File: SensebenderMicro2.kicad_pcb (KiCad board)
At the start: 2 copper layers, 19 x 32 mm, 39 parts, among them P1 Debug, P2 MYSX_1.2, P3 Antenna, Q1 SI2333DDS-T1-GE3, U1 ATSAMD21E, U2 MCP1703T-3302E, U3 NRF24L01, U4 RFM69HW, U5 ATSHA204A, U6 AT45DB041E, U7 Si7021, U8 AT24C32-STUM-T, Y1 32Khz

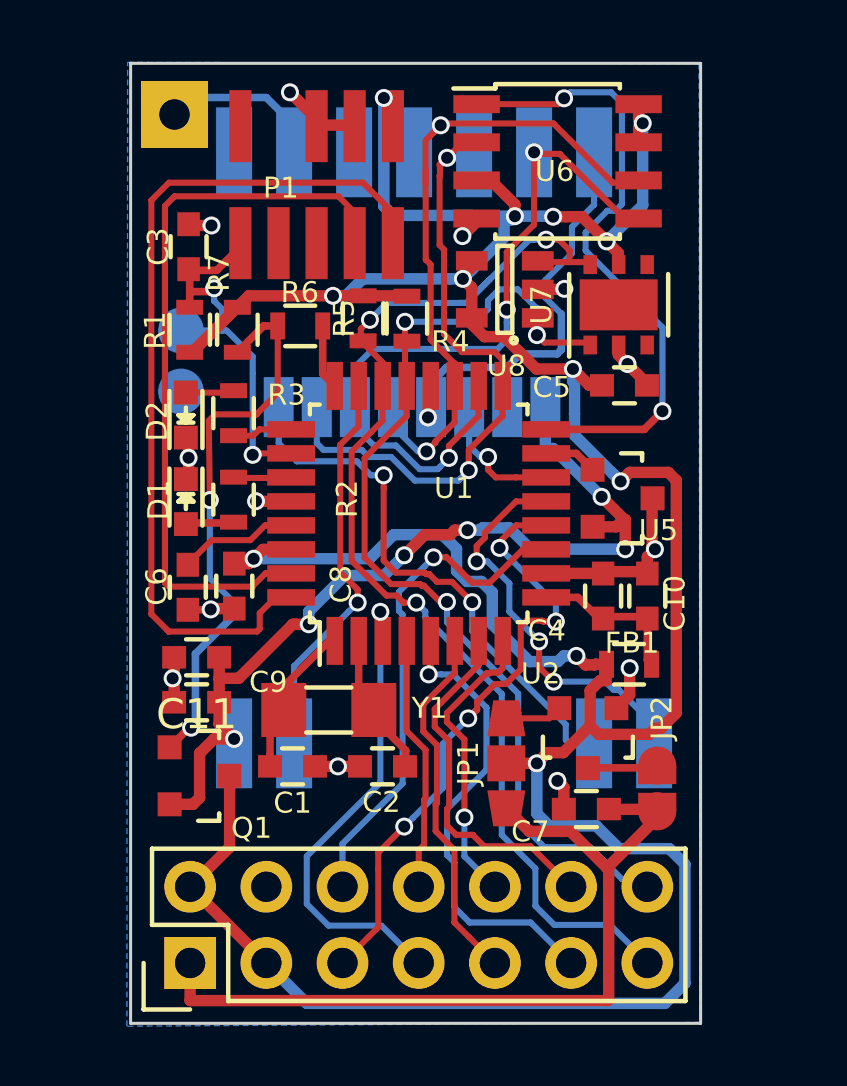
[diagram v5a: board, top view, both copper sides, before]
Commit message: Updated to use MYSX2.x with reset
Also shuffled peripherals around on the samd, to make routing easier
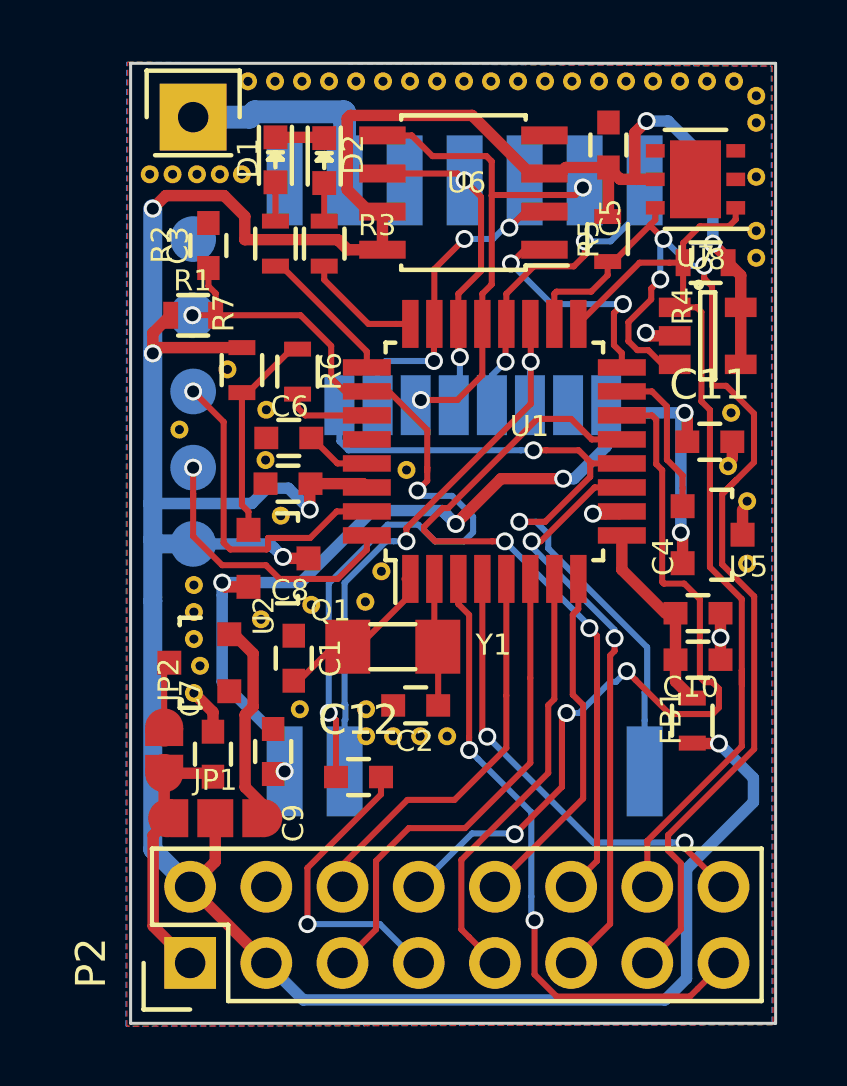
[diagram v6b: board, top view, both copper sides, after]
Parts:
- removed P1: Debug, mysensors_connectors:Cortex_M_Debug_Connector
- added C12: C, Capacitors_SMD:C_0603, F.Cu at (96.6, 105.8)
- added REF**: via-0.6mm, mysensors_obscurities:via-0.6mm, F.Cu at (108.9, 95.4)
- added REF**: via-0.6mm, mysensors_obscurities:via-0.6mm, F.Cu at (93.5, 93.5)
- added REF**: via-0.6mm, mysensors_obscurities:via-0.6mm, F.Cu at (93.5, 95.2)
- added REF**: via-0.6mm, mysensors_obscurities:via-0.6mm, F.Cu at (98.2, 95.6)
- added REF**: via-0.6mm, mysensors_obscurities:via-0.6mm, F.Cu at (99.6, 104.4)
- added REF**: via-0.6mm, mysensors_obscurities:via-0.6mm, F.Cu at (98.7, 104.4)
- added REF**: via-0.6mm, mysensors_obscurities:via-0.6mm, F.Cu at (97.8, 104.4)
- added REF**: via-0.6mm, mysensors_obscurities:via-0.6mm, F.Cu at (96.9, 104.4)
- added REF**: via-0.6mm, mysensors_obscurities:via-0.6mm, F.Cu at (92.2, 92.2)
- added REF**: via-0.6mm, mysensors_obscurities:via-0.6mm, F.Cu at (90.6, 94.2)
- added REF**: via-0.6mm, mysensors_obscurities:via-0.6mm, F.Cu at (91.1, 103.0)
- added REF**: via-0.6mm, mysensors_obscurities:via-0.6mm, F.Cu at (109.0, 93.6)
- added REF**: via-0.6mm, mysensors_obscurities:via-0.6mm, F.Cu at (91.3, 102.1)
- added REF**: via-0.6mm, mysensors_obscurities:via-0.6mm, F.Cu at (91.1, 101.2)
- added REF**: via-0.6mm, mysensors_obscurities:via-0.6mm, F.Cu at (91.1, 100.3)
- added REF**: via-0.6mm, mysensors_obscurities:via-0.6mm, F.Cu at (91.1, 99.4)
- added REF**: via-0.6mm, mysensors_obscurities:via-0.6mm, F.Cu at (97.4, 98.9)
- added REF**: via-0.6mm, mysensors_obscurities:via-0.6mm, F.Cu at (96.8, 99.9)
- added REF**: via-0.6mm, mysensors_obscurities:via-0.6mm, F.Cu at (93.3, 100.5)
- added REF**: via-0.6mm, mysensors_obscurities:via-0.6mm, F.Cu at (95.0, 100.1)
- added REF**: via-0.6mm, mysensors_obscurities:via-0.6mm, F.Cu at (96.9, 103.5)
- added REF**: via-0.6mm, mysensors_obscurities:via-0.6mm, F.Cu at (94.6, 103.5)
- added REF**: via-0.6mm, mysensors_obscurities:via-0.6mm, F.Cu at (109.6, 98.7)
- added REF**: via-0.6mm, mysensors_obscurities:via-0.6mm, F.Cu at (109.9, 83.1)
- added REF**: via-0.6mm, mysensors_obscurities:via-0.6mm, F.Cu at (109.1, 82.6)
- added REF**: via-0.6mm, mysensors_obscurities:via-0.6mm, F.Cu at (108.2, 82.6)
- added REF**: via-0.6mm, mysensors_obscurities:via-0.6mm, F.Cu at (107.3, 82.6)
- added REF**: via-0.6mm, mysensors_obscurities:via-0.6mm, F.Cu at (106.4, 82.6)
- added REF**: via-0.6mm, mysensors_obscurities:via-0.6mm, F.Cu at (105.5, 82.6)
- added REF**: via-0.6mm, mysensors_obscurities:via-0.6mm, F.Cu at (104.6, 82.6)
- added REF**: via-0.6mm, mysensors_obscurities:via-0.6mm, F.Cu at (103.7, 82.6)
- added REF**: via-0.6mm, mysensors_obscurities:via-0.6mm, F.Cu at (102.8, 82.6)
- added REF**: via-0.6mm, mysensors_obscurities:via-0.6mm, F.Cu at (101.9, 82.6)
- added REF**: via-0.6mm, mysensors_obscurities:via-0.6mm, F.Cu at (109.6, 96.6)
- added REF**: via-0.6mm, mysensors_obscurities:via-0.6mm, F.Cu at (101.0, 82.6)
- added REF**: via-0.6mm, mysensors_obscurities:via-0.6mm, F.Cu at (100.1, 82.6)
- added REF**: via-0.6mm, mysensors_obscurities:via-0.6mm, F.Cu at (99.2, 82.6)
- added REF**: via-0.6mm, mysensors_obscurities:via-0.6mm, F.Cu at (98.3, 82.6)
- added REF**: via-0.6mm, mysensors_obscurities:via-0.6mm, F.Cu at (97.4, 82.6)
- added REF**: via-0.6mm, mysensors_obscurities:via-0.6mm, F.Cu at (96.5, 82.6)
- added REF**: via-0.6mm, mysensors_obscurities:via-0.6mm, F.Cu at (95.6, 82.6)
- added REF**: via-0.6mm, mysensors_obscurities:via-0.6mm, F.Cu at (94.7, 82.6)
- added REF**: via-0.6mm, mysensors_obscurities:via-0.6mm, F.Cu at (93.8, 82.6)
- added REF**: via-0.6mm, mysensors_obscurities:via-0.6mm, F.Cu at (92.9, 82.6)
- added REF**: via-0.6mm, mysensors_obscurities:via-0.6mm, F.Cu at (109.9, 88.5)
- added REF**: via-0.6mm, mysensors_obscurities:via-0.6mm, F.Cu at (92.7, 85.7)
- added REF**: via-0.6mm, mysensors_obscurities:via-0.6mm, F.Cu at (92.0, 85.7)
- added REF**: via-0.6mm, mysensors_obscurities:via-0.6mm, F.Cu at (91.2, 85.7)
- added REF**: via-0.6mm, mysensors_obscurities:via-0.6mm, F.Cu at (90.4, 85.7)
- added REF**: via-0.6mm, mysensors_obscurities:via-0.6mm, F.Cu at (89.6, 85.7)
- added REF**: via-0.6mm, mysensors_obscurities:via-0.6mm, F.Cu at (109.9, 87.6)
- added REF**: via-0.6mm, mysensors_obscurities:via-0.6mm, F.Cu at (109.9, 85.8)
- added REF**: via-0.6mm, mysensors_obscurities:via-0.6mm, F.Cu at (109.9, 84.0)
- added REF**: via-0.6mm, mysensors_obscurities:via-0.6mm, F.Cu at (94.0, 97.1)
- added W1: GND, Measurement_Points:Measurement_Point_Round-SMD-Pad_Small, B.Cu at (91.1, 87.9)
- added W4: SWDIO, Measurement_Points:Measurement_Point_Round-SMD-Pad_Small, B.Cu at (91.1, 95.5)
- added W5: VCC, Measurement_Points:Measurement_Point_Round-SMD-Pad_Small, B.Cu at (91.1, 98.0)
- P2: value MYSX_1.2 -> MYSX_2.4; footprint mysensors_connectors:MYSX_1.3 -> mysensors_connectors:MYSX_2.4
- P3: moved to F.Cu
- W3: value GND -> SWCLK
- moved C11 18.6 mm to (108.3, 94.6), turned to 0 degrees
- moved JP2 16.5 mm to (90.1, 104.9)
- moved U2 13.2 mm to (91.3, 102.0), turned to 90 degrees
- moved C7 12.6 mm to (91.7, 105.0), turned to 90 degrees
- moved D1 11.8 mm to (93.8, 85.2)
- moved R4 10.1 mm to (108.2, 88.6), turned to 180 degrees
- moved JP1 9.87 mm to (91.8, 107.2), turned to 180 degrees
- moved D2 9.66 mm to (95.5, 85.2), turned to 270 degrees
- moved R2 8.65 mm to (93.8, 88.0), turned to 90 degrees
- moved R5 8.57 mm to (104.9, 87.9)
- moved C5 8.03 mm to (104.9, 84.7), turned to 270 degrees
- moved Q1 7.71 mm to (93.9, 98.5)
- moved U8 6.94 mm to (108.2, 91.1), turned to 0 degrees
- moved R3 6.41 mm to (95.5, 88.0)
- moved C6 6.01 mm to (94.3, 94.5), turned to 0 degrees
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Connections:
- net Net-(C10-Pad1) renamed +3.3VA
- P2 pad 7: /A1 -> /RST
- P2 pad 8: /A2 -> /LEGACY_ID
- U1 pad 11: /D2_DTM -> /D5_PWM
- U1 pad 12: /D1_DFM -> /IRQ
- U1 pad 13: /RFM_RESET -> /D6_PWM
- U1 pad 14: /NRF_CE -> /LEGACY_ID
- U1 pad 17: /MISO -> /D8_SDA
- U1 pad 18: /MOSI -> /D7_SCL
- U1 pad 19: /SCK -> /NRF_CE_RFM_DIO5
- U1 pad 21: /D8_SDA -> /MOSI
- U1 pad 22: /D7_SCL -> /SCK
- U1 pad 23: /RFM_DIO5 -> /MISO
- U1 pad 24: Net-(R6-Pad2) -> Net-(R3-Pad1)
- U1 pad 25: Net-(R3-Pad1) -> Net-(R2-Pad1)
- U1 pad 27: Net-(R2-Pad1) -> Net-(R6-Pad2)
- U1 pad 5: /D5_PWM -> /D2_DTM
- U1 pad 6: /D3_INT -> /D1_DFM
- U1 pad 7: /D6_PWM -> /D3_INT
- U3 pad 3: /NRF_CE -> /NRF_CE_RFM_DIO5
- U4 pad 1: /RFM_RESET -> Net-(U4-Pad1)
- U4 pad 7: /RFM_DIO5 -> /NRF_CE_RFM_DIO5
- W3 pad 1: GND -> /SWCLK
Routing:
- net /LEGACY_ID: track 0.00 -> 27.4 mm, vias 0 -> 3
- net /V_RAW: track 28.4 -> 8.80 mm
- net /SWDIO: track 29.3 -> 9.76 mm, vias 0 -> 1
- net /NRF_CE_RFM_DIO5: track 0.00 -> 19.4 mm, vias 0 -> 2
- net GND: track 24.9 -> 8.37 mm, vias 13 -> 3
- net /RESET: track 13.0 -> 29.2 mm, vias 2 -> 3
- net /SWCLK: track 24.7 -> 11.0 mm, vias 0 -> 1
- net /RFM_RESET: track 13.4 -> 0.00 mm, vias 3 -> 0
- net /FLS_CS: track 21.3 -> 7.95 mm
- net /RFM_DIO5: track 13.3 -> 0.00 mm, vias 1 -> 0
- net /SCK: track 24.2 -> 11.0 mm
- net /D6_PWM: track 12.0 -> 24.5 mm, vias 0 -> 2
- net Net-(Q1-Pad1): track 18.8 -> 7.12 mm, vias 2 -> 0
- net /RST: track 0.00 -> 10.2 mm, vias 0 -> 1
- net /MISO: track 21.6 -> 12.6 mm, vias 2 -> 3
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- added copper zone on F.Cu, net GND
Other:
- board size 19 x 32 mm -> 21.5 x 32 mm
- net class Antenna added: clearance 0.381, trace_width 0.762, via_dia 0.6, via_drill 0.4
- net class Default: clearance 0.1778 -> 0.1524
- rule trace_clearance: 0.1778 -> 0.1524
- rule trace_min: 0.1778 -> 0.1524

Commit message: updated silkscreen placements
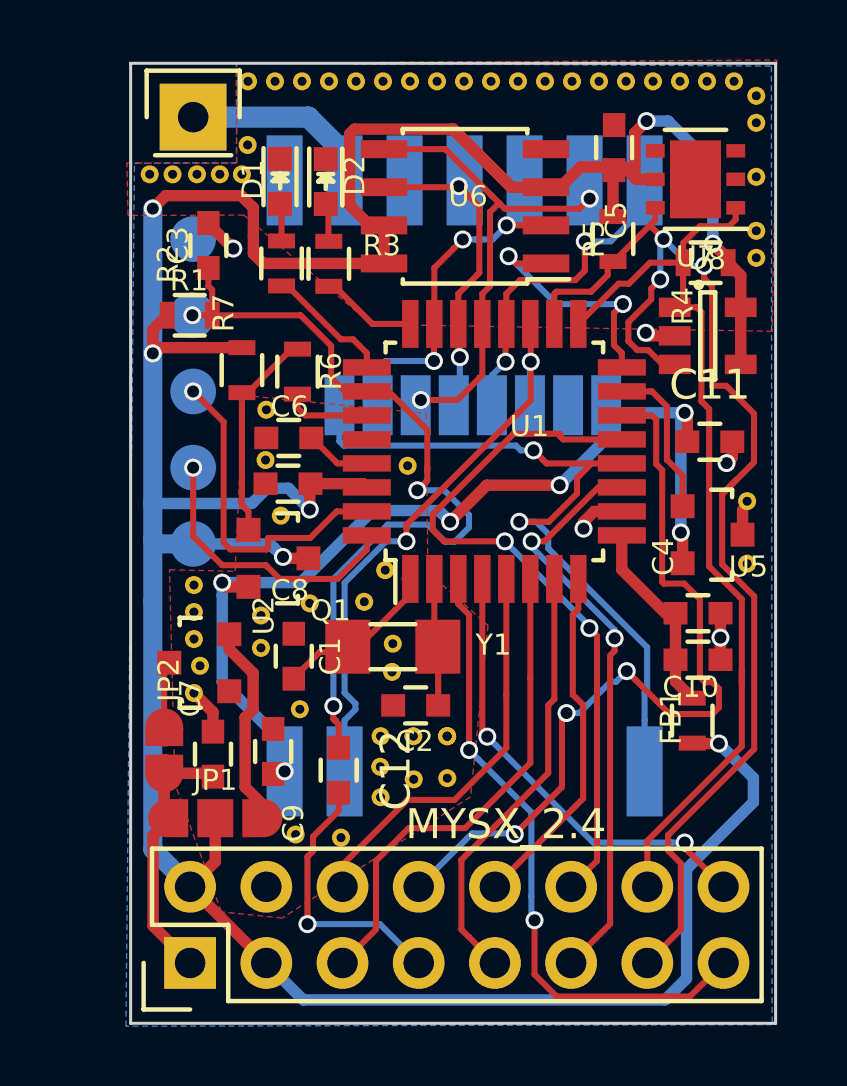
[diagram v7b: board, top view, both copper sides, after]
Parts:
- removed the REF** at (108.9, 95.4)
- removed the REF** at (96.9, 104.4)
- removed the REF** at (92.2, 92.2)
- removed the REF** at (90.6, 94.2)
- removed the REF** at (109.0, 93.6)
- removed the REF** at (96.9, 103.5)
- added REF**: via-0.6mm, mysensors_obscurities:via-0.6mm, F.Cu at (93.3, 101.5)
- added REF**: via-0.6mm, mysensors_obscurities:via-0.6mm, F.Cu at (97.7, 102.3)
- added REF**: via-0.6mm, mysensors_obscurities:via-0.6mm, F.Cu at (97.7, 101.3)
- added REF**: via-0.6mm, mysensors_obscurities:via-0.6mm, F.Cu at (96.0, 107.8)
- added REF**: via-0.6mm, mysensors_obscurities:via-0.6mm, F.Cu at (97.3, 106.5)
- added REF**: via-0.6mm, mysensors_obscurities:via-0.6mm, F.Cu at (97.3, 105.4)
- added REF**: via-0.6mm, mysensors_obscurities:via-0.6mm, F.Cu at (92.9, 84.7)
- added REF**: via-0.6mm, mysensors_obscurities:via-0.6mm, F.Cu at (94.5, 107.7)
- added REF**: via-0.6mm, mysensors_obscurities:via-0.6mm, F.Cu at (99.6, 105.8)
- added REF**: via-0.6mm, mysensors_obscurities:via-0.6mm, F.Cu at (98.4, 105.9)
- added REF**: via-0.6mm, mysensors_obscurities:via-0.6mm, F.Cu at (99.6, 104.4)
- moved REF** 2.75 mm to (101.4, 101.4)
- moved D1 0.73 mm to (94.0, 85.9)
- moved D2 0.70 mm to (95.5, 85.9)
- moved C12 0.70 mm to (95.9, 105.6), turned to 270 degrees
- moved R2 0.69 mm to (94.0, 88.7)
- moved R3 0.69 mm to (95.6, 88.7)
- moved U6 0.46 mm to (100.1, 86.8)
- moved REF** 0.42 mm to (97.3, 104.4)
- moved REF** 0.23 mm to (98.4, 104.4)
- moved C5 0.21 mm to (105.1, 84.8)
- moved R5 0.18 mm to (105.1, 87.9)
- moved REF** 0.14 mm to (98.2, 95.4)
- moved REF** 0.13 mm to (97.5, 98.9)
- moved REF** 0.13 mm to (93.3, 100.4)
- moved R1 0.12 mm to (91.0, 90.4)
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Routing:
- net +3V3: track 112.4 -> 115.8 mm
- net /RESET: track 29.2 -> 27.8 mm
- net /RST: track 10.2 -> 9.06 mm
- net Net-(P3-Pad1): track 7.39 -> 6.45 mm
- net /CSN: track 10.9 -> 11.7 mm
- net /D6_PWM: track 24.5 -> 23.8 mm
- net Net-(R3-Pad1): track 3.93 -> 3.24 mm
- net /MOSI: track 16.8 -> 16.2 mm
- net Net-(R2-Pad1): track 4.75 -> 4.25 mm
- net GND: track 8.37 -> 8.80 mm, vias 3 -> 5
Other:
- net class Antenna: clearance 0.381 -> 0.1; trace_width 0.762 -> 0.71

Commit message: recreated routing with better ground plane
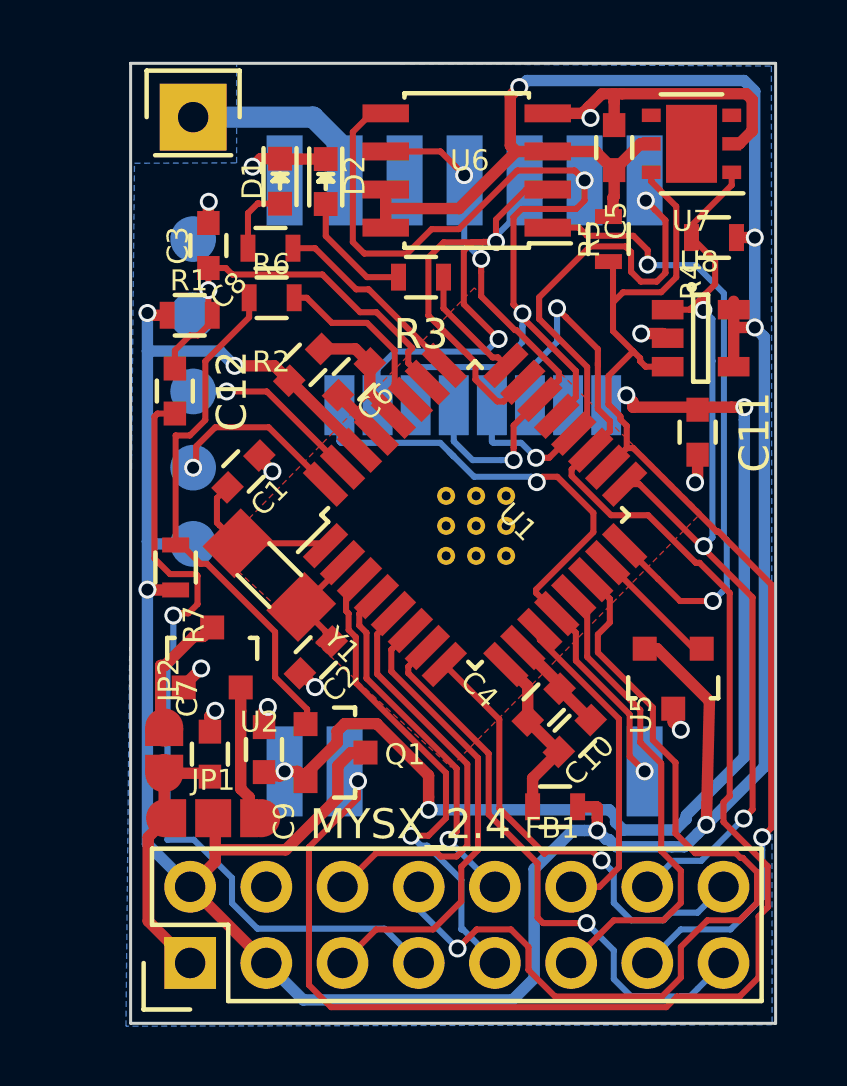
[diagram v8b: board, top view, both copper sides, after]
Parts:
- removed the REF** at (93.3, 101.5)
- removed the REF** at (97.7, 102.3)
- removed the REF** at (97.7, 101.3)
- removed the REF** at (109.6, 98.7)
- removed the REF** at (109.6, 96.6)
- removed the REF** at (109.9, 88.5)
- removed the REF** at (109.9, 87.6)
- removed the REF** at (109.9, 85.8)
- removed the REF** at (109.9, 84.0)
- removed the REF** at (94.0, 97.1)
- removed the REF** at (93.5, 93.5)
- removed the REF** at (96.0, 107.8)
- removed the REF** at (93.5, 95.2)
- removed the REF** at (98.2, 95.4)
- removed the REF** at (99.6, 104.4) (x2)
- removed the REF** at (98.4, 104.4)
- removed the REF** at (97.3, 104.4)
- removed the REF** at (91.1, 103.0)
- removed the REF** at (91.3, 102.1)
- removed the REF** at (91.1, 101.2)
- removed the REF** at (91.1, 100.3)
- removed the REF** at (91.1, 99.4)
- removed the REF** at (97.3, 106.5)
- removed the REF** at (97.5, 98.9)
- removed the REF** at (96.8, 99.9)
- removed the REF** at (93.3, 100.4)
- removed the REF** at (95.0, 100.0)
- removed the REF** at (94.6, 103.5)
- removed the REF** at (109.9, 83.1)
- removed the REF** at (109.1, 82.6)
- removed the REF** at (108.2, 82.6)
- removed the REF** at (107.3, 82.6)
- removed the REF** at (106.4, 82.6)
- removed the REF** at (97.3, 105.4)
- removed the REF** at (105.5, 82.6)
- removed the REF** at (104.6, 82.6)
- removed the REF** at (103.7, 82.6)
- removed the REF** at (102.8, 82.6)
- removed the REF** at (101.9, 82.6)
- removed the REF** at (101.0, 82.6)
- removed the REF** at (100.1, 82.6)
- removed the REF** at (99.2, 82.6)
- removed the REF** at (98.3, 82.6)
- removed the REF** at (97.4, 82.6)
- removed the REF** at (92.9, 84.7)
- removed the REF** at (96.5, 82.6)
- removed the REF** at (95.6, 82.6)
- removed the REF** at (94.7, 82.6)
- removed the REF** at (93.8, 82.6)
- removed the REF** at (92.9, 82.6)
- removed the REF** at (92.7, 85.7)
- removed the REF** at (92.0, 85.7)
- removed the REF** at (91.2, 85.7)
- removed the REF** at (90.4, 85.7)
- removed the REF** at (89.6, 85.7)
- removed the REF** at (94.5, 107.7)
- removed the REF** at (101.4, 101.4)
- removed the REF** at (99.6, 105.8)
- removed the REF** at (98.4, 105.9)
- added REF**: via-0.6mm, mysensors_obscurities:via-0.6mm, F.Cu at (101.5, 98.4)
- added REF**: via-0.6mm, mysensors_obscurities:via-0.6mm, F.Cu at (100.5, 98.4)
- added REF**: via-0.6mm, mysensors_obscurities:via-0.6mm, F.Cu at (99.5, 98.4)
- added REF**: via-0.6mm, mysensors_obscurities:via-0.6mm, F.Cu at (101.5, 97.4)
- added REF**: via-0.6mm, mysensors_obscurities:via-0.6mm, F.Cu at (100.5, 97.4)
- added REF**: via-0.6mm, mysensors_obscurities:via-0.6mm, F.Cu at (99.5, 97.4)
- added REF**: via-0.6mm, mysensors_obscurities:via-0.6mm, F.Cu at (101.5, 96.4)
- added REF**: via-0.6mm, mysensors_obscurities:via-0.6mm, F.Cu at (100.5, 96.4)
- added REF**: via-0.6mm, mysensors_obscurities:via-0.6mm, F.Cu at (99.5, 96.4)
- moved C12 13.8 mm to (90.5, 92.9)
- moved R7 6.94 mm to (90.5, 98.8), turned to 90 degrees
- moved Q1 6.75 mm to (95.8, 105.0)
- moved C1 6.38 mm to (92.8, 95.6), turned to 225 degrees
- moved C4 5.98 mm to (102.8, 103.4), turned to 225 degrees
- moved FB1 5.40 mm to (103.1, 106.8), turned to 180 degrees
- moved U5 4.98 mm to (107.1, 102.5), turned to 180 degrees
- moved C10 4.83 mm to (103.8, 104.4), turned to 45 degrees
- moved Y1 4.76 mm to (93.6, 99.1), turned to 315 degrees
- moved C8 4.00 mm to (94.8, 92.0), turned to 45 degrees
- moved C2 3.69 mm to (95.2, 101.8), turned to 45 degrees
- moved R3 3.11 mm to (98.7, 89.1), turned to 180 degrees
- moved C6 2.92 mm to (96.4, 92.5), turned to 225 degrees
- moved R6 2.61 mm to (93.7, 89.8), turned to 0 degrees
- moved U1 2.21 mm to (100.5, 97.1), turned to 45 degrees
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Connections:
- P2 pad 15: /A1 -> /D9_A3
- P2 pad 16: /A2 -> /D10_A4
- U1 pad 11: /D5_PWM -> /D6_PWM
- U1 pad 13: /D6_PWM -> /D5_PWM
- U1 pad 3: /A1 -> /D3_INT
- U1 pad 4: /A2 -> /D4_INT
- U1 pad 7: /D3_INT -> /D9_A3
- U1 pad 8: /D4_INT -> /D10_A4
- U5 pad 2: +3.3VP -> +3V3
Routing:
- net /NRF_CE_RFM_DIO5: track 19.6 -> 54.8 mm
- net /A1: track 21.3 -> 0.00 mm, vias 2 -> 0
- net /D9_A3: track 0.00 -> 19.4 mm, vias 0 -> 1
- net GND: track 8.80 -> 27.6 mm, vias 5 -> 11
- net /RST: track 9.06 -> 27.2 mm
- net /D10_A4: track 0.00 -> 15.7 mm, vias 0 -> 1
- net /A2: track 15.4 -> 0.00 mm, vias 2 -> 0
- net /MOSI: track 16.2 -> 31.3 mm
- net /RESET: track 27.8 -> 14.5 mm, vias 3 -> 1
- net /FLS_CS: track 8.16 -> 21.2 mm
- net /D6_PWM: track 23.8 -> 10.9 mm, vias 2 -> 0
- net /MISO: track 12.4 -> 25.2 mm, vias 3 -> 2
- net Net-(Q1-Pad1): track 7.12 -> 17.6 mm
- net +3V3: track 115.8 -> 125.9 mm, vias 7 -> 8
- net /CSN: track 11.7 -> 19.2 mm
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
